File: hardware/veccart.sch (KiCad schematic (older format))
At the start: 42 parts, among them CON1 vectrex-edge-connector, J1 USB_C_Receptacle_USB2.0, J2 Conn_01x06_Male, U1 LM1117-3.3, U2 STM32F411RCTx, U3 74HC32, U4 SN74LVC8T245DB, U5 W25Q128, Y1 8MHz

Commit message: PCB fingers fixes
- Fixes #10 removes soldermask ink around PCB fingers
- Fixes #11 Edge of PCB fingers should be 18.0mm from center of 3.52mm mounting hole and 1.2mm from edge, and slightly enlarged (0.2mm oversized)
- Also aligns holes, fingers and board outline on 0.1mm grid
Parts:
- CON1: footprint veccart:vectrex-edge-connector-thinner -> veccart:vectrex-edge-connector-thinner-no-soldermask; symbol veccart-rescue:vectrex-edge-connector -> veccart-rescue:vectrex-edge-connector-veccart-rescue
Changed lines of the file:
@@
 EESchema Schematic File Version 4
-LIBS:veccart-cache
 EELAYER 30 0
 EELAYER END
@@
 $EndDescr
 $Comp
-L veccart-rescue:GND #PWR07
+L veccart-rescue:GND-veccart-rescue #PWR07
 U 1 1 59F16914
 P 1700 5300
@@
 $EndComp
 $Comp
-L veccart-rescue:GND #PWR0101
+L veccart-rescue:GND-veccart-rescue #PWR0101
 U 1 1 5D00E463
 P 3850 6350
@@
 $EndComp
 $Comp
-L veccart-rescue:GND #PWR0102
+L veccart-rescue:GND-veccart-rescue #PWR0102
 U 1 1 5D00E892
 P 4600 6350
@@
 	4250 6200 4250 6350
 $Comp
-L veccart-rescue:GND #PWR0103
+L veccart-rescue:GND-veccart-rescue #PWR0103
 U 1 1 5D00F858
 P 4250 6350
@@
 USB-IN
 $Comp
-L veccart-rescue:GND #PWR0105
+L veccart-rescue:GND-veccart-rescue #PWR0105
 U 1 1 5D01B9D7
 P 5650 4300
@@
 $EndComp
 $Comp
-L veccart-rescue:GND #PWR0106
+L veccart-rescue:GND-veccart-rescue #PWR0106
 U 1 1 5D023148
 P 7250 3950
@@
 $EndComp
 $Comp
-L veccart-rescue:+5V #PWR0112
+L veccart-rescue:+5V-veccart-rescue #PWR0112
 U 1 1 5D05FE50
 P 7350 750
@@
 $EndComp
 $Comp
-L veccart-rescue:+5V #PWR0117
+L veccart-rescue:+5V-veccart-rescue #PWR0117
 U 1 1 5D06ED8C
 P 1750 1050
@@
 Connection ~ 4350 4750
 $Comp
-L veccart-rescue:GND #PWR0119
+L veccart-rescue:GND-veccart-rescue #PWR0119
 U 1 1 5D07FB9D
 P 4700 4850
@@
 	8150 1900 8150 2000
 $Comp
-L veccart-rescue:GND #PWR0124
+L veccart-rescue:GND-veccart-rescue #PWR0124
 U 1 1 5D0A1129
 P 8150 2000
@@
 $EndComp
 $Comp
-L veccart-rescue:GND #PWR0126
+L veccart-rescue:GND-veccart-rescue #PWR0126
 U 1 1 5D0F5289
 P 9800 2150
@@
 $EndComp
 $Comp
-L veccart-rescue:+5V #PWR0127
+L veccart-rescue:+5V-veccart-rescue #PWR0127
 U 1 1 5D0F55E9
 P 9800 1150
@@
 $EndComp
 $Comp
-L veccart-rescue:+5V #PWR0128
+L veccart-rescue:+5V-veccart-rescue #PWR0128
 U 1 1 5D0F60DC
 P 3850 5900
@@
 	10500 1400 10350 1400
 $Comp
-L veccart-rescue:GND #PWR0130
+L veccart-rescue:GND-veccart-rescue #PWR0130
 U 1 1 5D0AE42B
 P 10350 1400
@@
 USB-IN
 $Comp
-L veccart-rescue:GND #PWR0118
+L veccart-rescue:GND-veccart-rescue #PWR0118
 U 1 1 5DEA6FB0
 P 1700 7400
@@
 $EndComp
 $Comp
-L veccart-rescue:GND #PWR0131
+L veccart-rescue:GND-veccart-rescue #PWR0131
 U 1 1 5DEA771E
 P 1400 7400
@@
 	3250 6200 3100 6200
 $Comp
-L veccart-rescue:GND #PWR0132
+L veccart-rescue:GND-veccart-rescue #PWR0132
 U 1 1 5DF1039D
 P 3450 6100
@@
 SDAT
 $Comp
-L veccart-rescue:GND #PWR0135
+L veccart-rescue:GND-veccart-rescue #PWR0135
 U 1 1 5E1C4F53
 P 7700 5250
@@
 $EndComp
 $Comp
-L veccart-rescue:+5V #PWR0136
+L veccart-rescue:+5V-veccart-rescue #PWR0136
 U 1 1 5E1C55CA
 P 7700 4650
@@
 $EndComp
 $Comp
-L veccart-rescue:GND #PWR0137
+L veccart-rescue:GND-veccart-rescue #PWR0137
 U 1 1 5E1CFFED
 P 8350 5250
@@
 $EndComp
 $Comp
-L veccart-rescue:+5V #PWR0138
+L veccart-rescue:+5V-veccart-rescue #PWR0138
 U 1 1 5E1CFFF7
 P 8350 4650
@@
 	5100 3150 4950 3150
 $Comp
-L veccart-rescue:GND #PWR0133
+L veccart-rescue:GND-veccart-rescue #PWR0133
 U 1 1 5E222AFD
 P 9000 5250
@@
 $EndComp
 $Comp
-L veccart-rescue:+5V #PWR0134
+L veccart-rescue:+5V-veccart-rescue #PWR0134
 U 1 1 5E222B03
 P 9000 4650
@@
 $EndComp
 $Comp
-L veccart-rescue:GND #PWR0139
+L veccart-rescue:GND-veccart-rescue #PWR0139
 U 1 1 5E22D72D
 P 9650 5250
@@
 $EndComp
 $Comp
-L veccart-rescue:+5V #PWR0140
+L veccart-rescue:+5V-veccart-rescue #PWR0140
 U 1 1 5E22D733
 P 9650 4650
@@
 $EndComp
 $Comp
-L veccart-rescue:GND #PWR0141
+L veccart-rescue:GND-veccart-rescue #PWR0141
 U 1 1 5E232EFC
 P 10300 5250
@@
 $EndComp
 $Comp
-L veccart-rescue:+5V #PWR0142
+L veccart-rescue:+5V-veccart-rescue #PWR0142
 U 1 1 5E232F02
 P 10300 4650
@@
 $EndComp
 $Comp
-L veccart-rescue:GND #PWR0143
+L veccart-rescue:GND-veccart-rescue #PWR0143
 U 1 1 5E237D78
 P 7700 6300
@@
 $EndComp
 $Comp
-L veccart-rescue:+5V #PWR0144
+L veccart-rescue:+5V-veccart-rescue #PWR0144
 U 1 1 5E237D7E
 P 7700 5700
@@
 $EndComp
 $Comp
-L veccart-rescue:GND #PWR0145
+L veccart-rescue:GND-veccart-rescue #PWR0145
 U 1 1 5E23C8F2
 P 8350 6300
@@
 $EndComp
 $Comp
-L veccart-rescue:+5V #PWR0146
+L veccart-rescue:+5V-veccart-rescue #PWR0146
 U 1 1 5E23C8F8
 P 8350 5700
@@
 $EndComp
 $Comp
-L veccart-rescue:GND #PWR0147
+L veccart-rescue:GND-veccart-rescue #PWR0147
 U 1 1 5E241687
 P 9000 6300
@@
 $EndComp
 $Comp
-L veccart-rescue:+5V #PWR0148
+L veccart-rescue:+5V-veccart-rescue #PWR0148
 U 1 1 5E24168D
 P 9000 5700
@@
 $EndComp
 $Comp
-L veccart-rescue:GND #PWR0149
+L veccart-rescue:GND-veccart-rescue #PWR0149
 U 1 1 5E247B45
 P 9650 6300
@@
 $EndComp
 $Comp
-L veccart-rescue:+5V #PWR0150
+L veccart-rescue:+5V-veccart-rescue #PWR0150
 U 1 1 5E247B4B
 P 9650 5700
@@
 $EndComp
 $Comp
-L veccart-rescue:GND #PWR0151
+L veccart-rescue:GND-veccart-rescue #PWR0151
 U 1 1 5E24CDAA
 P 10300 6300
@@
 $EndComp
 $Comp
-L veccart-rescue:+5V #PWR0152
+L veccart-rescue:+5V-veccart-rescue #PWR0152
 U 1 1 5E24CDB0
 P 10300 5700
@@
 Connection ~ 6700 7300
 $Comp
-L veccart-rescue:GND #PWR0153
+L veccart-rescue:GND-veccart-rescue #PWR0153
 U 1 1 5E4F4996
 P 6700 7500
@@
 $EndComp
 $Comp
-L veccart-rescue:vectrex-edge-connector CON1
+L veccart-rescue:vectrex-edge-connector-veccart-rescue CON1
 U 1 1 59F1631A
 P 1800 3500
 F 0 "CON1" H 1450 5350 60  0000 C CNN
 F 1 "vectrex-edge-connector" V 1400 3250 60  0000 C CNN
-F 2 "veccart:vectrex-edge-connector-thinner" H 1800 4200 60  0001 C CNN
+F 2 "veccart:vectrex-edge-connector-thinner-no-soldermask" H 1800 4200 60  0001 C CNN
 F 3 "" H 1800 4200 60  0001 C CNN
 	1    1800 3500
@@
 $EndComp
 $Comp
-L veccart-rescue:GND #PWR0154
+L veccart-rescue:GND-veccart-rescue #PWR0154
 U 1 1 5DEB047F
 P 6800 5250
@@
 $EndComp
 $Comp
-L veccart-rescue:+5V #PWR0155
+L veccart-rescue:+5V-veccart-rescue #PWR0155
 U 1 1 5DEB5A91
 P 6800 4950

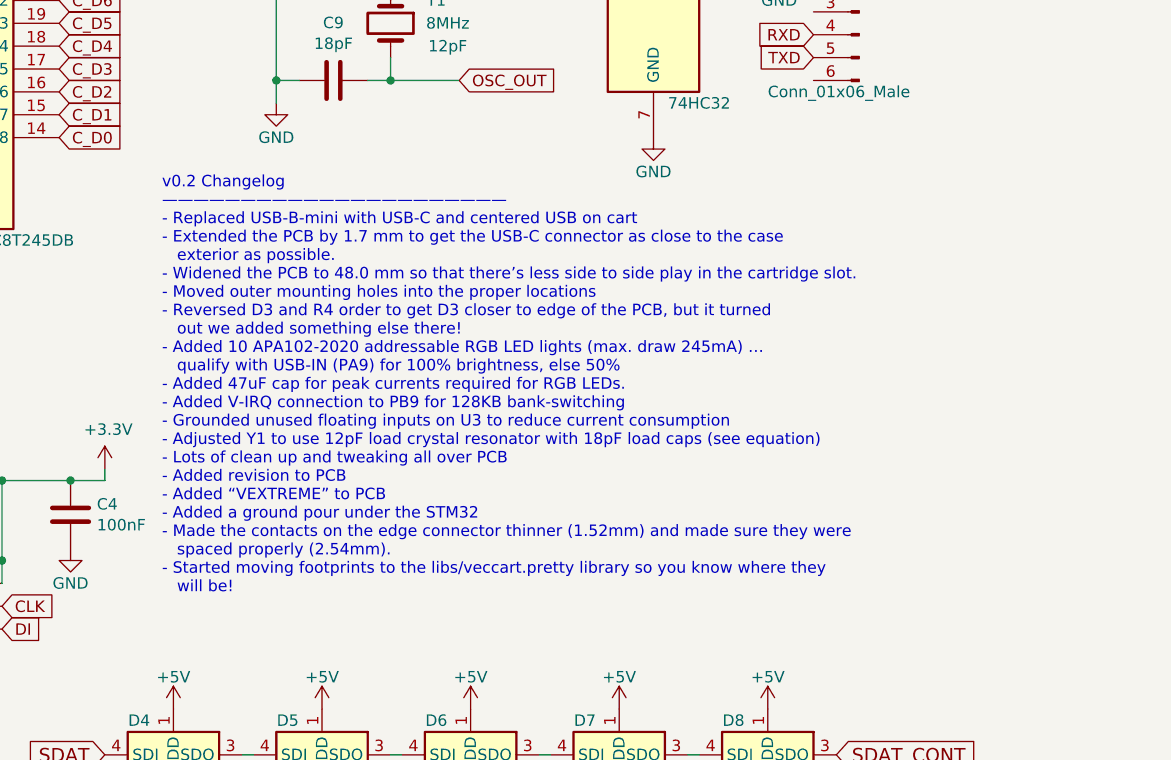
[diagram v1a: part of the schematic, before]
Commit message: Fixes #17, make all pads on addressable LEDS the same size
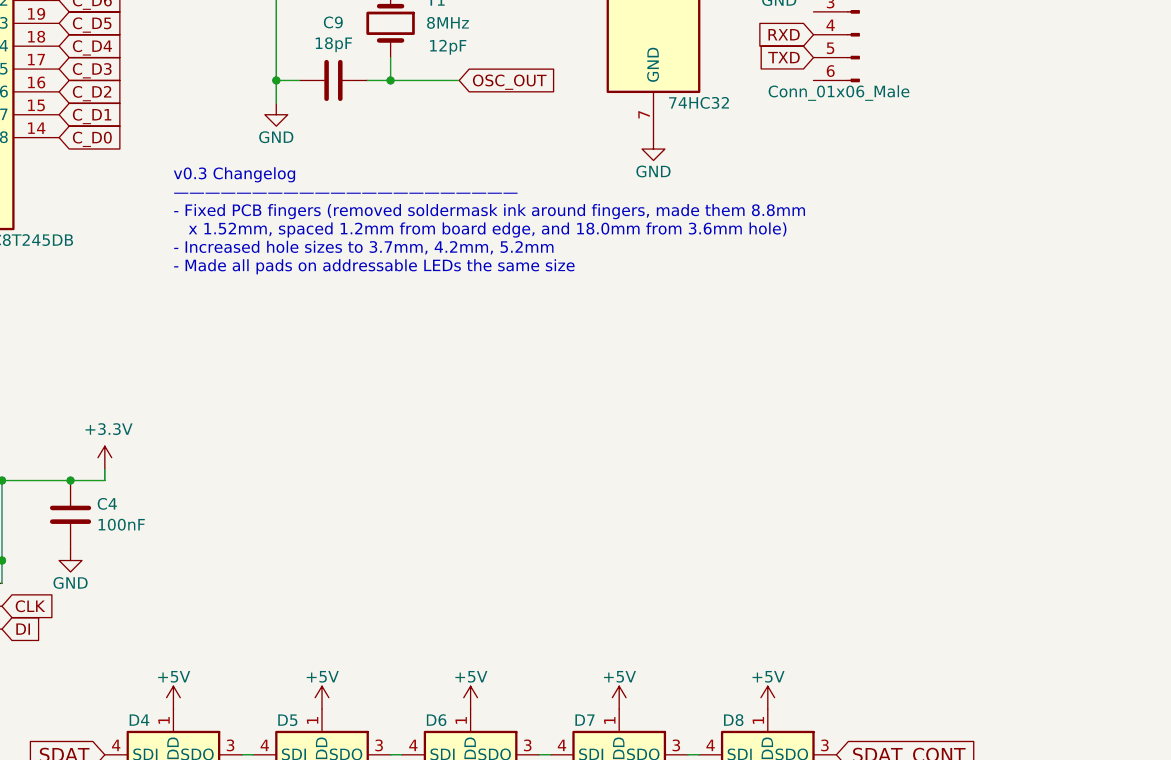
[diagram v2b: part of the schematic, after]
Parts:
- D10, D11, D12, D13, D4, D5, D6, D7, D8, D9: footprint veccart:LED-APA102-2020_6 -> veccart:LED-APA102-2020_6_REV_2
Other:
- note added: "v0.3 Changelog\n——————————————————————\n- Fixed PCB fingers (removed soldermask ink around fingers, made them 8.8mm\n x 1.52mm, spaced 1.2mm from board edge, and 18.0mm from 3.6mm hole)\n- Increased hole sizes to 3.7mm, 4.2mm, 5.2mm\n- Made all pads on addressable LEDs the same size\n"
- note removed: "v0.2 Changelog\n——————————————————————\n- Replaced USB-B-mini with USB-C and centered USB on cart\n- Extended the PCB by 1.7 mm to get the USB-C connector as close to the case\n exterior as possible.\n- Widened the PCB to 48.0 mm so that there’s less side to side play in the cartridge slot.\n- Moved outer mounting holes into the proper locations\n- Reversed D3 and R4 order to get D3 closer to edg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"
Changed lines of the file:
@@
 Title "VEXTREME Vectrex Multicart"
 Date "2019-12-01"
-Rev "v0.2"
+Rev "v0.3"
 Comp ""
 Comment1 ""
@@
 Wire Wire Line
 	6700 6500 6700 6300
-Text Notes 7650 4150 0    50   ~ 0
-v0.2 Changelog\n——————————————————————\n- Replaced USB-B-mini with USB-C and centered USB on cart\n- Extended the PCB by 1.7 mm to get the USB-C connector as close to the case\n   exterior as possible.\n- Widened the PCB to 48.0 mm so that there’s less side to side play in the cartridge slot.\n- Moved outer mounting holes into the proper locations\n- Reversed D3 and R4 order to get D3 closer to edge of the PCB, but it turned\n   out we added something else there!\n- Added 10 APA102-2020 addressable RGB LED lights (max. draw 245mA) …\n   qualify with USB-IN (PA9) for 100% brightness, else 50%\n- Added 47uF cap for peak currents required for RGB LEDs.\n- Added V-IRQ connection to PB9 for 128KB bank-switching\n- Grounded unused floating inputs on U3 to reduce current consumption\n- Adjusted Y1 to use 12pF load crystal resonator with 18pF load caps (see equation)\n- Lots of clean up and tweaking all over PCB\n- Added revision to PCB\n- Added “VEXTREME” to PCB\n- Added a ground pour under the STM32\n- Made the contacts on the edge connector thinner (1.52mm) and made sure they were\n   spaced properly (2.54mm).\n- Started moving footprints to the libs/veccart.pretty library so you know where they \n   will be!
+Text Notes 7700 2750 0    50   ~ 0
+v0.3 Changelog\n——————————————————————\n- Fixed PCB fingers (removed soldermask ink around fingers, made them 8.8mm\n   x 1.52mm, spaced 1.2mm from board edge, and 18.0mm from 3.6mm hole)\n- Increased hole sizes to 3.7mm, 4.2mm, 5.2mm\n- Made all pads on addressable LEDs the same size\n
 Text Notes 8000 900  0    50   ~ 0
 CL = (C8 * C9)/(C8 + C9) + Cstray\n(324pF/36pF) + 4pF = 13pF (close to 12pF Y1 CL requirement)\n
@@
 F 0 "D13" H 10150 6250 50  0000 C CNN
 F 1 "APA102-2020" H 10600 5750 50  0000 C CNN
-F 2 "veccart:LED-APA102-2020_6" H 10350 5700 50  0001 L TNN
+F 2 "veccart:LED-APA102-2020_6_REV_2" H 10350 5700 50  0001 L TNN
 F 3 "http://www.led-color.com/upload/201604/APA102-2020%20SMD%20LED.pdf" H 10400 5625 50  0001 L TNN
 	1    10300 6000
@@
 F 0 "D12" H 9500 6250 50  0000 C CNN
 F 1 "APA102-2020" H 9950 5750 50  0000 C CNN
-F 2 "veccart:LED-APA102-2020_6" H 9700 5700 50  0001 L TNN
+F 2 "veccart:LED-APA102-2020_6_REV_2" H 9700 5700 50  0001 L TNN
 F 3 "http://www.led-color.com/upload/201604/APA102-2020%20SMD%20LED.pdf" H 9750 5625 50  0001 L TNN
 	1    9650 6000
@@
 F 0 "D11" H 8850 6250 50  0000 C CNN
 F 1 "APA102-2020" H 9300 5750 50  0000 C CNN
-F 2 "veccart:LED-APA102-2020_6" H 9050 5700 50  0001 L TNN
+F 2 "veccart:LED-APA102-2020_6_REV_2" H 9050 5700 50  0001 L TNN
 F 3 "http://www.led-color.com/upload/201604/APA102-2020%20SMD%20LED.pdf" H 9100 5625 50  0001 L TNN
 	1    9000 6000
@@
 F 0 "D10" H 8200 6250 50  0000 C CNN
 F 1 "APA102-2020" H 8650 5750 50  0000 C CNN
-F 2 "veccart:LED-APA102-2020_6" H 8400 5700 50  0001 L TNN
+F 2 "veccart:LED-APA102-2020_6_REV_2" H 8400 5700 50  0001 L TNN
 F 3 "http://www.led-color.com/upload/201604/APA102-2020%20SMD%20LED.pdf" H 8450 5625 50  0001 L TNN
 	1    8350 6000
@@
 F 0 "D9" H 7550 6250 50  0000 C CNN
 F 1 "APA102-2020" H 8000 5750 50  0000 C CNN
-F 2 "veccart:LED-APA102-2020_6" H 7750 5700 50  0001 L TNN
+F 2 "veccart:LED-APA102-2020_6_REV_2" H 7750 5700 50  0001 L TNN
 F 3 "http://www.led-color.com/upload/201604/APA102-2020%20SMD%20LED.pdf" H 7800 5625 50  0001 L TNN
 	1    7700 6000
@@
 F 0 "D8" H 10150 5200 50  0000 C CNN
 F 1 "APA102-2020" H 10600 4700 50  0000 C CNN
-F 2 "veccart:LED-APA102-2020_6" H 10350 4650 50  0001 L TNN
+F 2 "veccart:LED-APA102-2020_6_REV_2" H 10350 4650 50  0001 L TNN
 F 3 "http://www.led-color.com/upload/201604/APA102-2020%20SMD%20LED.pdf" H 10400 4575 50  0001 L TNN
 	1    10300 4950
@@
 F 0 "D7" H 9500 5200 50  0000 C CNN
 F 1 "APA102-2020" H 9950 4700 50  0000 C CNN
-F 2 "veccart:LED-APA102-2020_6" H 9700 4650 50  0001 L TNN
+F 2 "veccart:LED-APA102-2020_6_REV_2" H 9700 4650 50  0001 L TNN
 F 3 "http://www.led-color.com/upload/201604/APA102-2020%20SMD%20LED.pdf" H 9750 4575 50  0001 L TNN
 	1    9650 4950
@@
 F 0 "D6" H 8850 5200 50  0000 C CNN
 F 1 "APA102-2020" H 9300 4700 50  0000 C CNN
-F 2 "veccart:LED-APA102-2020_6" H 9050 4650 50  0001 L TNN
+F 2 "veccart:LED-APA102-2020_6_REV_2" H 9050 4650 50  0001 L TNN
 F 3 "http://www.led-color.com/upload/201604/APA102-2020%20SMD%20LED.pdf" H 9100 4575 50  0001 L TNN
 	1    9000 4950
@@
 F 0 "D5" H 8200 5200 50  0000 C CNN
 F 1 "APA102-2020" H 8650 4700 50  0000 C CNN
-F 2 "veccart:LED-APA102-2020_6" H 8400 4650 50  0001 L TNN
+F 2 "veccart:LED-APA102-2020_6_REV_2" H 8400 4650 50  0001 L TNN
 F 3 "http://www.led-color.com/upload/201604/APA102-2020%20SMD%20LED.pdf" H 8450 4575 50  0001 L TNN
 	1    8350 4950
@@
 F 0 "D4" H 7550 5200 50  0000 C CNN
 F 1 "APA102-2020" H 8000 4700 50  0000 C CNN
-F 2 "veccart:LED-APA102-2020_6" H 7750 4650 50  0001 L TNN
+F 2 "veccart:LED-APA102-2020_6_REV_2" H 7750 4650 50  0001 L TNN
 F 3 "http://www.led-color.com/upload/201604/APA102-2020%20SMD%20LED.pdf" H 7800 4575 50  0001 L TNN
 	1    7700 4950
